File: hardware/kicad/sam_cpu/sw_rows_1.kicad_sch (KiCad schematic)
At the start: 47 parts, among them J1 J1 SWITCH COLUMNS, Q11 MMBT3904, Q12 MMBT3904, Q13 MMBT3904, Q14 MMBT3904, Q15 MMBT3904, Q16 MMBT3904, Q17 MMBT3904, Q18 MMBT3904, U14 74HC165, U15 74HC165, U16 74HC165, U17 74HC165, U18 74HC165, U19 74HC165, U20 74HC595

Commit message: Redraw the schematic with wires (draft 0.2)
Every connection is now a wire, and each connector sits on the page of the
parts that drive or read it (Pi header with the RP2354B, J6/J12 with their
comparators and 74HC165, J1 with the 74HC595, J2/J3/J13 with their filters).
Signals between pages use global labels with page references. The Pi page is
merged into the MCU page; the Pi 4 sits on the 40-pin header J21.

ERC: 0 errors, 1 warning. Netlist check: 1266 pins, 299 nets, no differences.

Co-Authored-By: Claude Opus 5.5 (1M context) <noreply@anthropic.com>
Claude-Session: https://claude.ai/code/session_019DLTv1F2PjepjxqiUcAMKV
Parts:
- removed C80, C81, C82, C83, C84, C85, C86, C87, C88, C89, C90, C91, C92, C93, C94: 100n, Capacitor_SMD:C_0603_1608Metric, symbol Device:C
- removed J1: J1 SWITCH COLUMNS, Connector_Molex:Molex_KK-254_AE-6410-09A_1x09_P2.54mm_Vertical, symbol Connector_Generic:Conn_01x09
- removed Q11, Q12, Q13, Q14, Q15, Q16, Q17, Q18: MMBT3904, Package_TO_SOT_SMD:SOT-23, symbol Transistor_BJT:MMBT3904
- removed R168, R169, R170, R171, R172, R173, R174, R175, R176, R177, R178, R179, R180, R181, R182, R183: 1k, Resistor_SMD:R_0603_1608Metric, symbol Device:R
- removed U14, U15, U16, U17, U18: 74HC165, Package_SO:SOIC-16_3.9x9.9mm_P1.27mm, symbol 74xx:74HC165
- removed U20: 74HC595, Package_SO:SOIC-16_3.9x9.9mm_P1.27mm, symbol 74xx:74HC595
- added C43, C44, C45, C46, C47, C48, C49, C50, C51, C52, C53: 100n, Capacitor_SMD:C_0603_1608Metric, symbol Device:C
- added C54: 22u, Capacitor_SMD:C_0805_2012Metric, symbol Device:C
- added D11, D12, D13, D14, D15, D16, D17, D18: 1N4148W, Diode_SMD:D_SOD-123, symbol Diode:1N4148W
- added J6: J6 SWITCH ROWS, Connector_Molex:Molex_KK-254_AE-6410-10A_1x10_P2.54mm_Vertical, symbol Connector_Generic:Conn_01x10
- added R43, R46, R49, R52, R55, R58, R61, R64: 1k, Resistor_SMD:R_0603_1608Metric, symbol Device:R
- added R44, R47, R50, R53, R56, R59, R62, R65: 220, Resistor_SMD:R_0603_1608Metric, symbol Device:R
- added R45, R48, R51, R54, R57, R60, R63, R66: 10k, Resistor_SMD:R_0603_1608Metric, symbol Device:R
- added R67, R68: 3.3k, Resistor_SMD:R_0603_1608Metric, symbol Device:R
- added U8, U9: LM339, Package_SO:SOIC-14_3.9x8.7mm_P1.27mm, symbol Comparator:LM339
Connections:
- net +3V3: now also C53.1, R45.1, R48.1, R51.1, R54.1, R57.1, R60.1, R63.1, R66.1
- net +4V5: now also C51.1, C52.1, R43.1, R46.1, R49.1, R52.1, R55.1, R58.1, R61.1, R64.1, R67.1, U8.3 (V+), U9.3 (V+)
- net GND: now also C43.2, C44.2, C45.2, C46.2, C47.2, C48.2, C49.2, C50.2, C51.2, C52.2, C53.2, C54.2, J6.10 (Pin_10), R68.2, U8.12 (V-), U9.12 (V-)
- net RET1: no longer names the net of U19.11 (D0)
- net RET1: now also R45.2, U8.2
- net RET2: no longer names the net of U19.12 (D1)
- net RET2: now also R48.2, U8.1
- net RET3: no longer names the net of U19.13 (D2)
- net RET3: now also R51.2, U8.13
- net RET4: no longer names the net of U19.14 (D3)
- net RET4: now also R54.2, U8.14
- net RET5: no longer names the net of U19.3 (D4)
- net RET5: now also R57.2, U9.2
- net RET6: no longer names the net of U19.4 (D5)
- net RET6: now also R60.2, U9.1
- net RET7: no longer names the net of U19.5 (D6)
- net RET7: now also R63.2, U9.13
- net RET8: no longer names the net of U19.6 (D7)
- net RET8: now also R66.2, U9.14
- new net: D15.2 (A), R55.2, R56.1
- new net: C47.1, R56.2, U9.5 (+)
- new net: C49.1, R62.2, U9.11 (+)
- new net: D13.1 (K), J6.3 (Pin_3)
- new net: D13.2 (A), R49.2, R50.1
- new net: C48.1, R59.2, U9.7 (+)
- new net: D12.2 (A), R46.2, R47.1
- new net: C44.1, R47.2, U8.7 (+)
- new net: D11.1 (K), J6.1 (Pin_1)
- new net: D12.1 (K), J6.2 (Pin_2)
- new net: D14.1 (K), J6.5 (Pin_5)
- new net: D15.1 (K), J6.6 (Pin_6)
- new net: D16.1 (K), J6.7 (Pin_7)
- new net: D17.1 (K), J6.8 (Pin_8)
- new net: D18.1 (K), J6.9 (Pin_9)
- new net: C43.1, R44.2, U8.5 (+)
- new net: D16.2 (A), R58.2, R59.1
- new net: D18.2 (A), R64.2, R65.1
- new net: C50.1, R65.2, U9.9 (+)
- new net: D14.2 (A), R52.2, R53.1
- new net: C45.1, R50.2, U8.11 (+)
- new net: C46.1, R53.2, U8.9 (+)
- new net: D11.2 (A), R43.2, R44.1
- new net: D17.2 (A), R61.2, R62.1
- new net VREF: C54.1, R67.2, R68.1, U8.10 (-), U8.4 (-), U8.6 (-), U8.8 (-), U9.10 (-), U9.4 (-), U9.6 (-), U9.8 (-)
- no-connect marks 8 -> 2
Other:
- note added: "Comparator reference (2.25 V)"
- note added: "Per return (ARCHITECTURE.md 5.2-5.3): series diode from the connector, 1 k pull-up to +4.5 V, 220 R + 100 nF, LM339 against VREF (2.25 V). Output 1 = open, 0 = closed, as the ROM expects. Connector pin order follows the original drawing: check it with a meter."
- note removed: "74HC165 input chain (3.3 V)"
- note removed: "74HC595 strobe register"
- note removed: "J1: switch columns (strobes), key pin 2"
- note removed: "One shift clock for both registers: PIO1 shifts 48 inputs in while the next strobe pattern shifts into the 595 (ARCHITECTURE.md 5.3-5.4). First bits out of SW_DATA: U19 RET1-8, U18 RET9-16, U17 D1-8, U16 D9-16, U15 D17-24, U14 DIP1-8. Strobes: 595 high -> MMBT3904 on -> strobe pulled low (active), with the original 1 k pull-up to +4.5 V and 100 nF."
- note removed: "Strobe drivers 1-4"
- note removed: "Strobe drivers 5-8"
- title: Switch scan: 6 x 74HC165, 74HC595 strobes, J1 switch columns -> Switch matrix returns 1-8: J6, LM339 front end, 74HC165

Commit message: Use 3.96 mm KK-396 footprints for the switch harness connectors
J1, J2, J3, J6, J12 and J13 are 0.156" headers on the original board, so
the existing harness plugs need KK-396, as already used for J10 and J11.

Co-Authored-By: Claude Opus 5.5 (1M context) <noreply@anthropic.com>
Claude-Session: https://claude.ai/code/session_019DLTv1F2PjepjxqiUcAMKV
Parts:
- J6: footprint Connector_Molex:Molex_KK-254_AE-6410-10A_1x10_P2.54mm_Vertical -> Connector_Molex:Molex_KK-396_A-41791-0010_1x10_P3.96mm_Vertical
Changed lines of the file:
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@@
 			)
 		)
-		(property "Footprint" "Connector_Molex:Molex_KK-254_AE-6410-10A_1x10_P2.54mm_Vertical"
+		(property "Footprint" "Connector_Molex:Molex_KK-396_A-41791-0010_1x10_P3.96mm_Vertical"
 			(at 20.32 147.32 0)
 			(hide yes)

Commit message: Add RTC, test points and stereo speaker connector; place all parts on 2 layers
Schematic: DS3231MZ real-time clock on the Pi I2C1 with a CR2032 holder,
22 test points (rails, bus, strobes, switch chain, VREF, DAC outputs) and
J22, a second KK-396 speaker connector with L and R as separate pairs.
ERC 0 errors, generated netlist matches the intended nets.

PCB: 2 copper layers. The RP2354B sits near J9 with its USB-C on the top
edge 13 mm from the USB pins; decoupling, regulator and crystal parts on
their pins; every other part grouped by sheet next to its connector, low
parts only under the Pi. J17 and J22 on the right edge; Pi and J5 12 mm
lower to fit the audio parts.

Co-Authored-By: Claude Opus 5.5 (1M context) <noreply@anthropic.com>
Claude-Session: https://claude.ai/code/session_01ExuDVoDDDHhVWjb8EwVzYb
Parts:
- added TP19: VREF, TestPoint:TestPoint_Pad_D1.5mm, symbol Connector:TestPoint
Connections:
- net VREF: now also TP19.1
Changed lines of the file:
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@@
 	)
 	(junction
+		(at 210.82 228.6)
+		(diameter 0)
+		(color 0 0 0 0)
+	)
+	(junction
 		(at 91.44 190.5)
 		(diameter 0)
@@
 	(wire
 		(pts
+			(xy 233.68 215.9) (xy 233.68 213.36)
+		)
+		(stroke
+			(width 0)
+			(type default)
+		)
+	)
+	(wire
+		(pts
 			(xy 86.36 101.6) (xy 93.98 101.6)
 		)
@@
 	(wire
 		(pts
+			(xy 210.82 228.6) (xy 210.82 215.9)
+		)
+		(stroke
+			(width 0)
+			(type default)
+		)
+	)
+	(wire
+		(pts
+			(xy 210.82 215.9) (xy 233.68 215.9)
+		)
+		(stroke
+			(width 0)
+			(type default)
+		)
+	)
+	(wire
+		(pts
 			(xy 58.42 73.66) (xy 66.04 73.66)
 		)
@@
 					(unit 1)
 				)
+			)
+		)
+	)
+	(symbol
+		(lib_id "Connector:TestPoint")
+		(at 233.68 213.36 0)
+		(unit 1)
+		(body_style 1)
+		(exclude_from_sim no)
+		(in_bom yes)
+		(on_board yes)
+		(in_pos_files yes)
+		(dnp no)
+		(property "Reference" "TP19"
+			(at 233.68 206.502 0)
+			(show_name no)
+			(do_not_autoplace no)
+			(effects
+				(font
+					(size 1.27 1.27)
+				)
+			)
+		)
+		(property "Value" "VREF"
+			(at 233.68 208.28 0)
+			(show_name no)
+			(do_not_autoplace no)
+			(effects
+				(font
+					(size 1.27 1.27)
+				)
+			)
+		)
+		(property "Footprint" "TestPoint:TestPoint_Pad_D1.5mm"
+			(at 238.76 213.36 0)
+			(hide yes)
+			(show_name no)
+			(do_not_autoplace no)
+			(effects
+				(font
+					(size 1.27 1.27)
+				)
+			)
+		)
+		(property "Datasheet" ""
+			(at 238.76 213.36 0)
+			(hide yes)
+			(show_name no)
+			(do_not_autoplace no)
+			(effects
+				(font
+					(size 1.27 1.27)
+				)
+			)
+		)
+		(property "Description" "test point"
+			(at 233.68 213.36 0)
+			(hide yes)
+			(show_name no)
+			(do_not_autoplace no)
+			(effects
+				(font
+					(size 1.27 1.27)
+				)
+			)
+		)
+		(pin "1"
+		)
+		(instances
+			(project "sam_cpu"
+				(path "/2aea4fdf-a573-57d0-a5af-7bd6ce737647/5eeea8c2-b047-5ab4-84ef-a141605efbc1"
+					(reference "TP19")
+					(unit 1)
+				)

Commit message: Audio on external 12 V with TDA7297 stereo + subwoofer amps, NCP1117, guide regulator layout
- Remove the +-12 V input from J11; J23 external +12 V with polyfuse and TVS
- Replace the two TDA2030A with a TDA7297 bridge amp for left/right (J10, J22)
  and a second TDA7297 for the subwoofer (J24), fed by an (L+R)/2 110 Hz
  Sallen-Key low-pass (OPA1678); shared standby and RP2354B-controlled mute
- AMS1117 -> NCP1117-3.3 (ceramic-stable, as in the RP2350 guide), 10 uF 1206
- L1 and crystal part numbers from the RP2350 hardware guide
- Place the core regulator parts by hand following the Pico 2 layout; amps in a
  row with a heatsink keep-out; J23/J22/J24 on the right edge

Co-Authored-By: Claude Opus 5.5 (1M context) <noreply@anthropic.com>
Claude-Session: https://claude.ai/code/session_01ExuDVoDDDHhVWjb8EwVzYb
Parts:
- removed TP19: VREF, TestPoint:TestPoint_Pad_D1.5mm, symbol Connector:TestPoint
- added TP18: VREF, TestPoint:TestPoint_Pad_D1.5mm, symbol Connector:TestPoint
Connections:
- net VREF: now also TP18.1
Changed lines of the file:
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@@
+	)
+	(symbol
+		(lib_id "Connector:TestPoint")
+		(at 233.68 213.36 0)
+		(unit 1)
+		(body_style 1)
+		(exclude_from_sim no)
+		(in_bom yes)
+		(on_board yes)
+		(in_pos_files yes)
+		(dnp no)
+		(property "Reference" "TP18"
+			(at 233.68 206.502 0)
+			(show_name no)
+			(do_not_autoplace no)
+			(effects
+				(font
+					(size 1.27 1.27)
+				)
+			)
+		)
+		(property "Value" "VREF"
+			(at 233.68 208.28 0)
+			(show_name no)
+			(do_not_autoplace no)
+			(effects
+				(font
+					(size 1.27 1.27)
+				)
+			)
+		)
+		(property "Footprint" "TestPoint:TestPoint_Pad_D1.5mm"
+			(at 238.76 213.36 0)
+			(hide yes)
+			(show_name no)
+			(do_not_autoplace no)
+			(effects
+				(font
+					(size 1.27 1.27)
+				)
+			)
+		)
+		(property "Datasheet" ""
+			(at 238.76 213.36 0)
+			(hide yes)
+			(show_name no)
+			(do_not_autoplace no)
+			(effects
+				(font
+					(size 1.27 1.27)
+				)
+			)
+		)
+		(property "Description" "test point"
+			(at 233.68 213.36 0)
+			(hide yes)
+			(show_name no)
+			(do_not_autoplace no)
+			(effects
+				(font
+					(size 1.27 1.27)
+				)
+			)
+		)
+		(pin "1"
+		)
+		(instances
+			(project "sam_cpu"
+				(path "/2aea4fdf-a573-57d0-a5af-7bd6ce737647/5eeea8c2-b047-5ab4-84ef-a141605efbc1"
+					(reference "TP18")
+					(unit 1)
+				)
+			)
+		)
 	)
 	(symbol
@@
 					(unit 1)
 				)
-			)
-		)
-	)
-	(symbol
-		(lib_id "Connector:TestPoint")
-		(at 233.68 213.36 0)
-		(unit 1)
-		(body_style 1)
-		(exclude_from_sim no)
-		(in_bom yes)
-		(on_board yes)
-		(in_pos_files yes)
-		(dnp no)
-		(property "Reference" "TP19"
-			(at 233.68 206.502 0)
-			(show_name no)
-			(do_not_autoplace no)
-			(effects
-				(font
-					(size 1.27 1.27)
-				)
-			)
-		)
-		(property "Value" "VREF"
-			(at 233.68 208.28 0)
-			(show_name no)
-			(do_not_autoplace no)
-			(effects
-				(font
-					(size 1.27 1.27)
-				)
-			)
-		)
-		(property "Footprint" "TestPoint:TestPoint_Pad_D1.5mm"
-			(at 238.76 213.36 0)
-			(hide yes)
-			(show_name no)
-			(do_not_autoplace no)
-			(effects
-				(font
-					(size 1.27 1.27)
-				)
-			)
-		)
-		(property "Datasheet" ""
-			(at 238.76 213.36 0)
-			(hide yes)
-			(show_name no)
-			(do_not_autoplace no)
-			(effects
-				(font
-					(size 1.27 1.27)
-				)
-			)
-		)
-		(property "Description" "test point"
-			(at 233.68 213.36 0)
-			(hide yes)
-			(show_name no)
-			(do_not_autoplace no)
-			(effects
-				(font
-					(size 1.27 1.27)
-				)
-			)
-		)
-		(pin "1"
-		)
-		(instances
-			(project "sam_cpu"
-				(path "/2aea4fdf-a573-57d0-a5af-7bd6ce737647/5eeea8c2-b047-5ab4-84ef-a141605efbc1"
-					(reference "TP19")
-					(unit 1)
-				)

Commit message: Add two HD DMD panels on a PIO parallel bus (incremental edit)
RP2354B GPIO20-36 drive two HUB75 panels (J25/J26) through 3 x 74AHCT245
with shared CLK/LAT/OE and A/B row lines; J5 shares DMD_D0-D6. The 165
load and 595 latch share GPIO17; coin door moves to a 7th 165 (U30),
LED_STATUS and GI_SPARE to a new first 595 (U31). Board widened to 142 mm
below the Pi. Sheets and board edited in place via tools/changes, no
existing footprint moved.

Co-Authored-By: Claude Opus 5.5 (1M context) <noreply@anthropic.com>
Claude-Session: https://claude.ai/code/session_01ExuDVoDDDHhVWjb8EwVzYb
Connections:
- net SW_DATA renamed CHAIN6
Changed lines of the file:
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@@
 		)
 	)
-	(global_label "SW_DATA"
+	(global_label "CHAIN6"
 		(shape output)
 		(at 195.58 132.08 0)

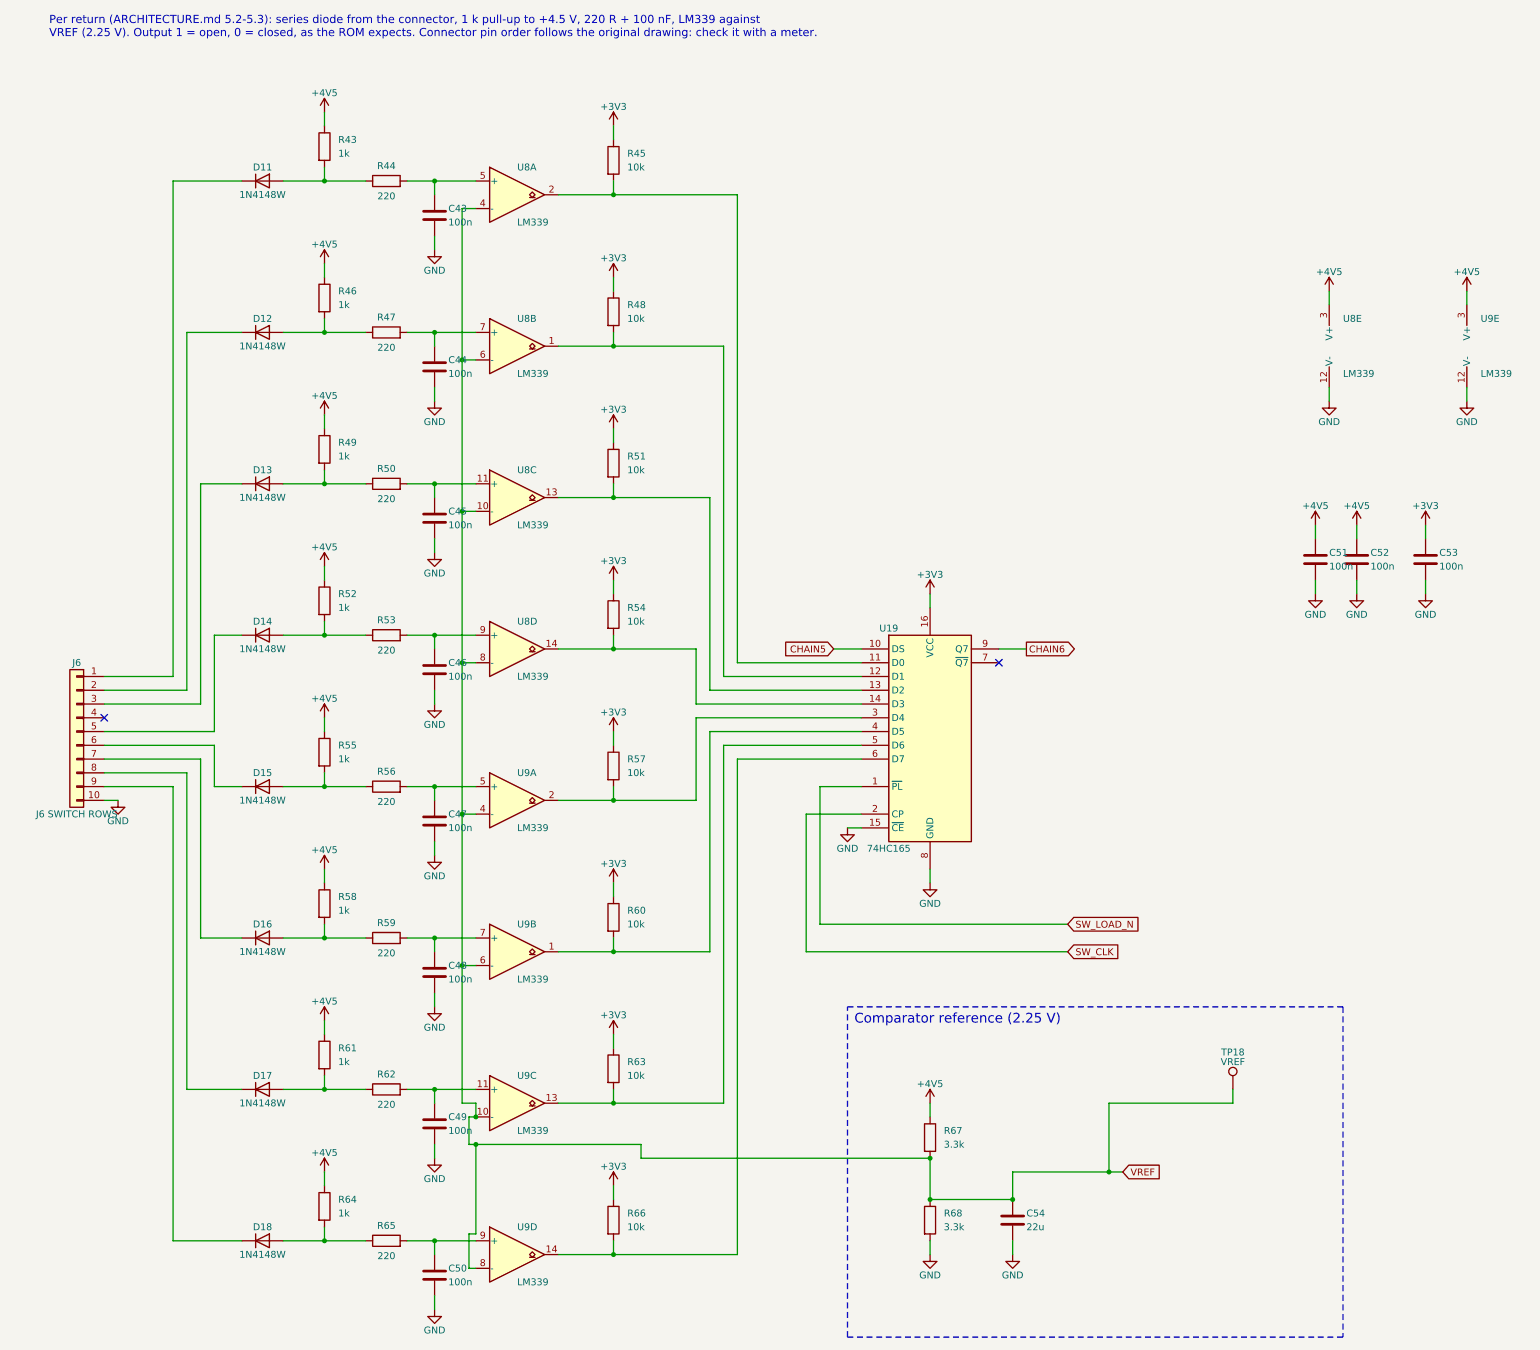
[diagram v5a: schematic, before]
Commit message: DIP switch block not loaded; larger schematic text
c30: SW3, R168-R175, U14 and C93 flagged DNP (schematic and board).
c31: schematic text 1.27 -> 1.6 mm (pins 1.5 mm), intersheet refs moved out.

Co-Authored-By: Claude Opus 5.5 (1M context) <noreply@anthropic.com>
Claude-Session: https://claude.ai/code/session_01ExuDVoDDDHhVWjb8EwVzYb
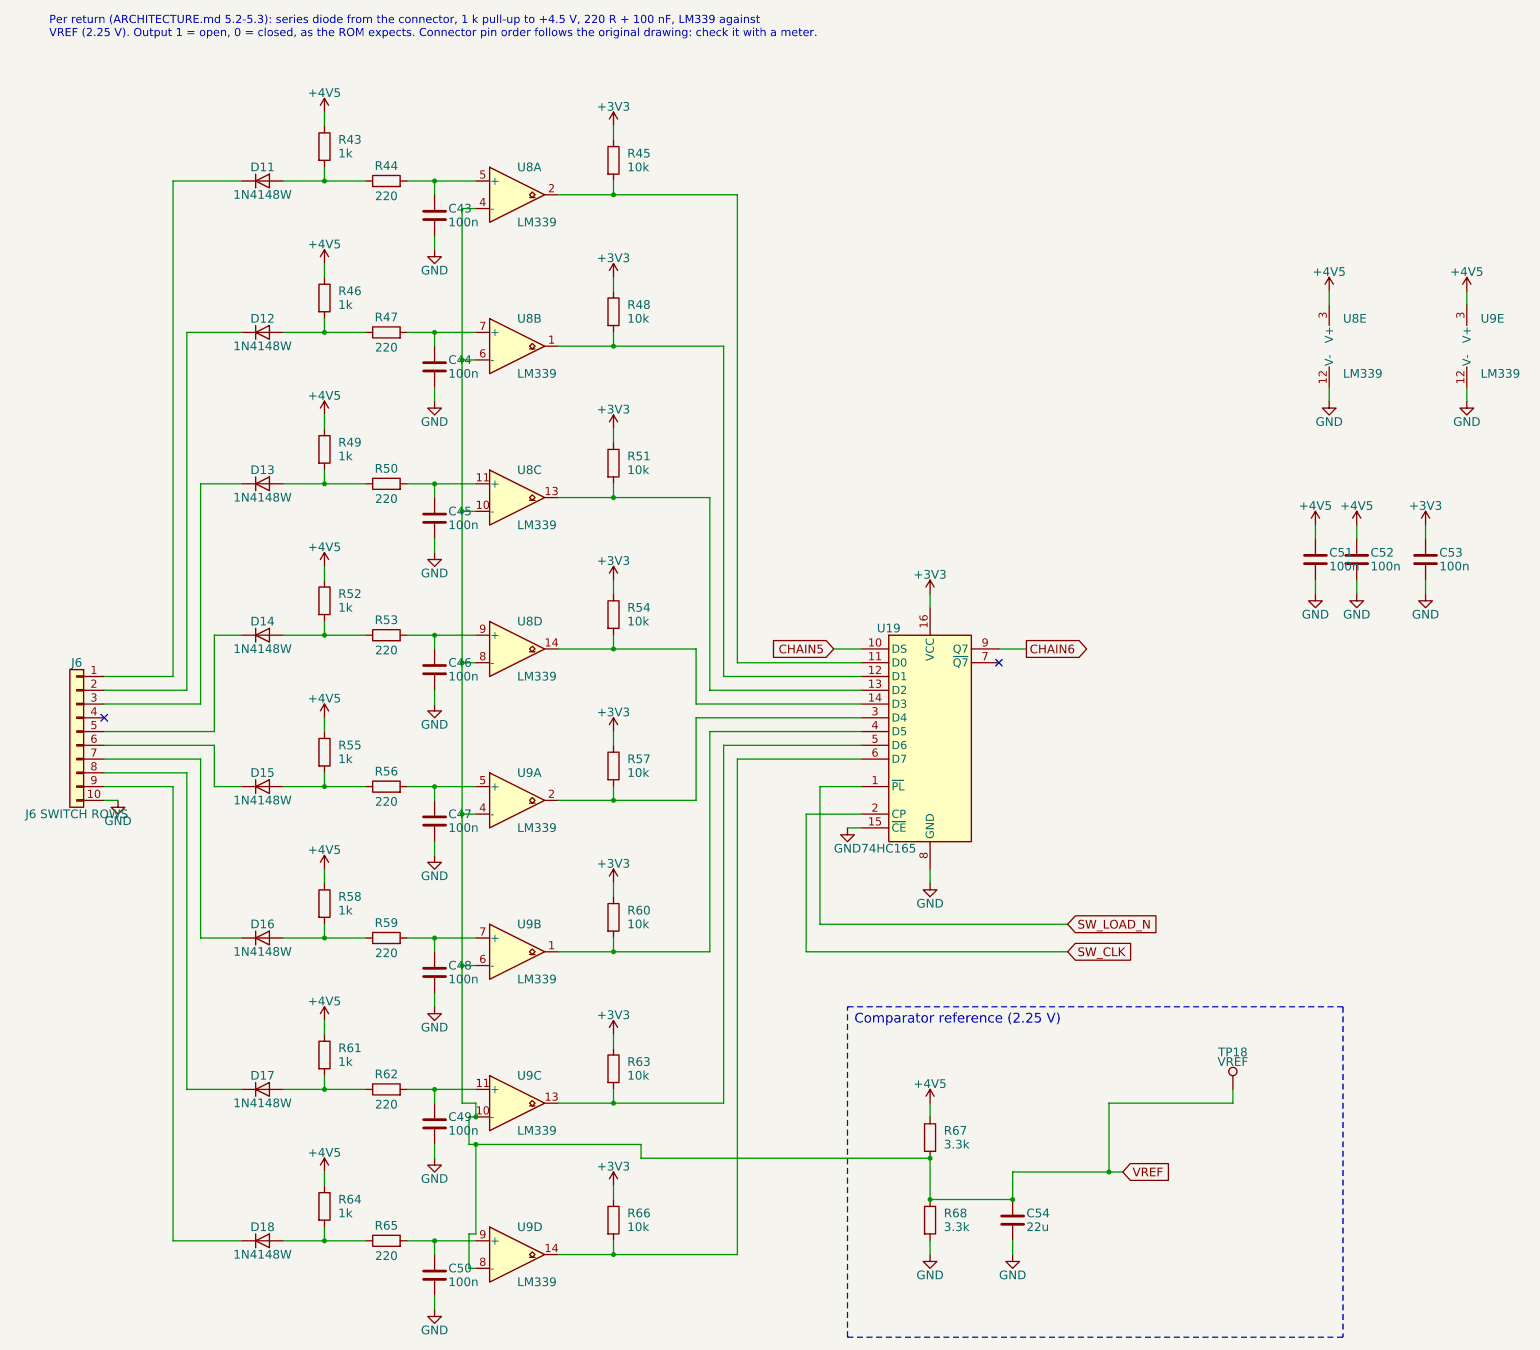
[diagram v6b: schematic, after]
